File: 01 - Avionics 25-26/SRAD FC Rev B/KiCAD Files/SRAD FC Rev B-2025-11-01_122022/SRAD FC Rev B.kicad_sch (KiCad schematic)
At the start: 0 parts

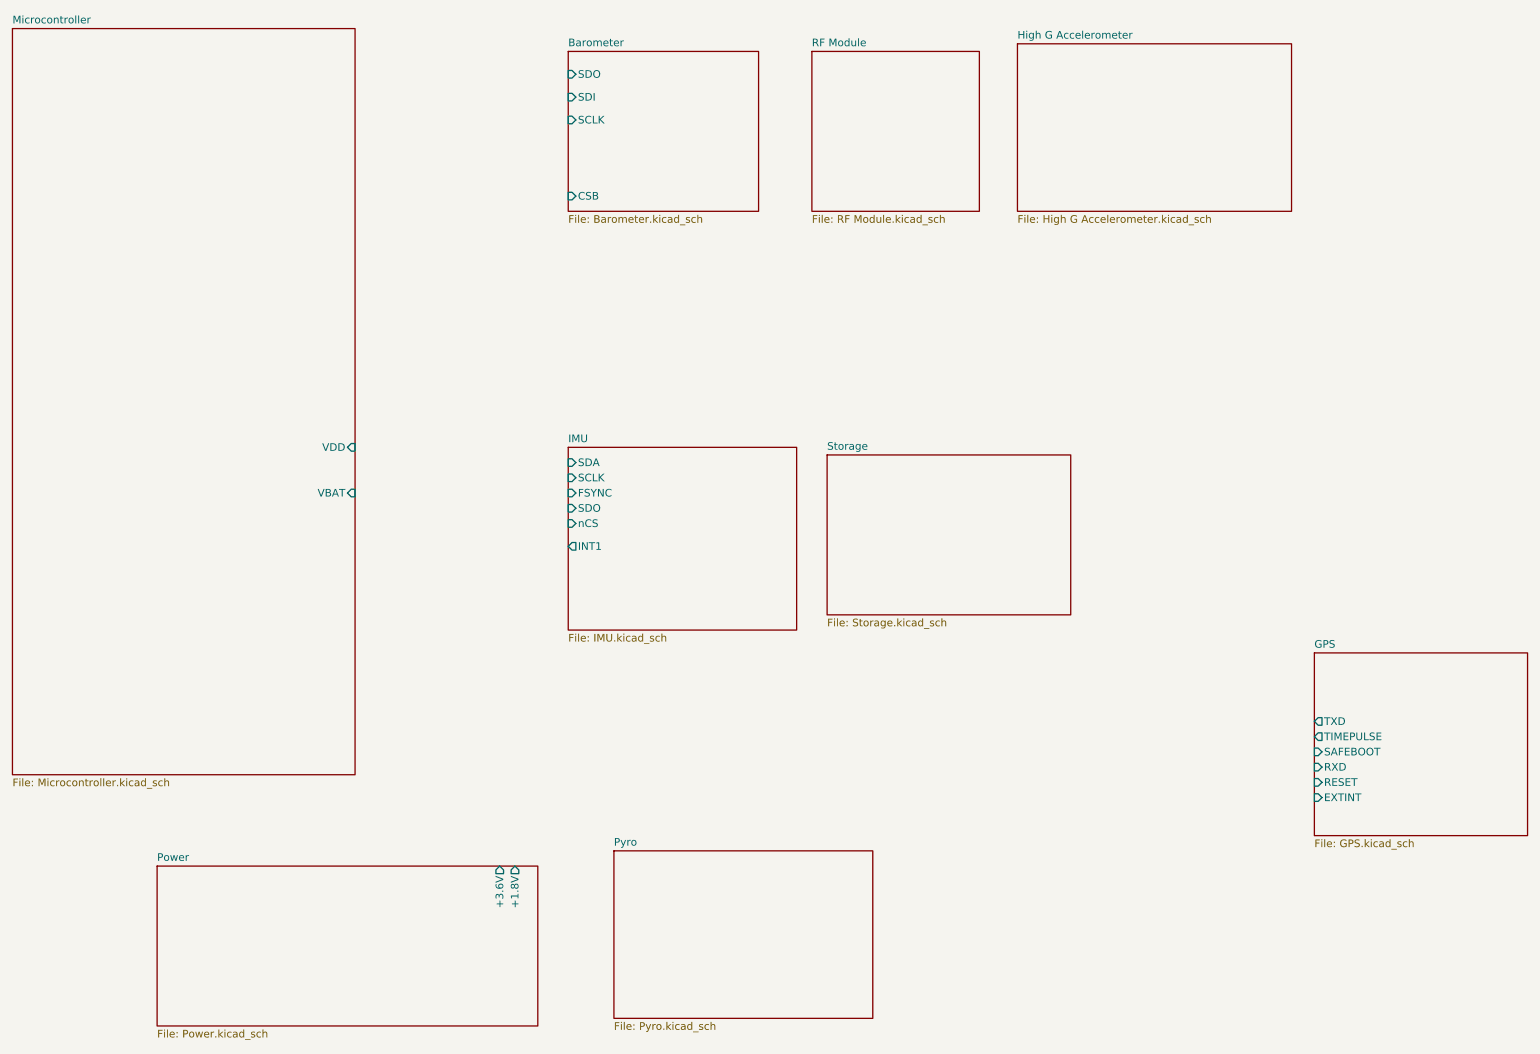
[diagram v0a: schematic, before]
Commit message: Added IMU and Barometer Circuits w/Root Symbols
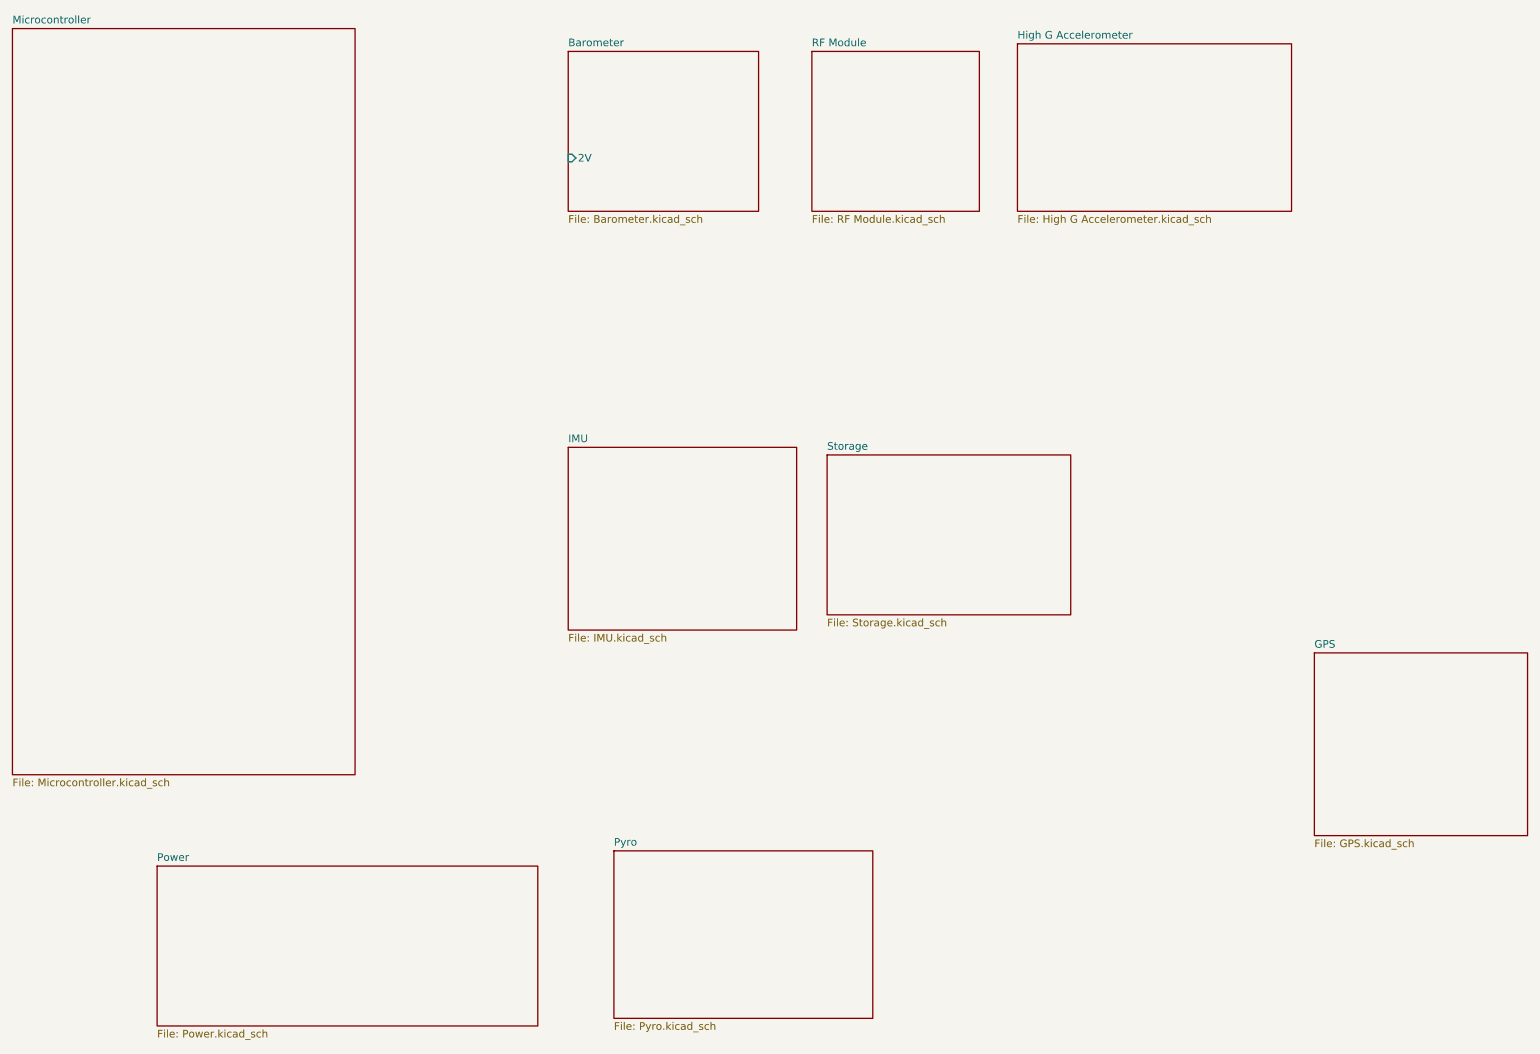
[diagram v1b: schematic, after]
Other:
- sheet Barometer ports: added 2V; removed CSB, SCLK, SDI, SDO
- sheet GPS ports: added none; removed EXTINT, RESET, RXD, SAFEBOOT, TIMEPULSE, TXD
- sheet IMU ports: added none; removed FSYNC, INT1, SCLK, SDA, SDO, nCS
- sheet Microcontroller ports: added none; removed VBAT, VDD
- sheet Power ports: added none; removed +1.8V, +3.6V
- company: Missouri S&T Rocket Design Team -> (none)
- title: SRAD FC Revision B -> (none)
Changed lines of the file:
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@@
 	(generator_version "9.0")
 	(paper "A4")
-	(title_block
-		(title "SRAD FC Revision B")
-		(date "2025-11-01")
-		(rev "B")
-		(company "Missouri S&T Rocket Design Team")
-		(comment 1 "Author(s): Aaron Brinker, Isaac Lough, Joseph Hinchie, Ryan Newey, and Ian Butrick")
-	)
 	(sheet
 		(at 45.72 162.56)
@@
 			)
 		)
-		(pin "+3.6V" output
-			(at 102.87 162.56 90)
-			(effects
-				(font
-					(size 1.27 1.27)
-				)
-				(justify right)
-			)
-		)
-		(pin "+1.8V" output
-			(at 105.41 162.56 90)
-			(effects
-				(font
-					(size 1.27 1.27)
-				)
-				(justify right)
-			)
-		)
 		(instances
 			(project "SRAD FC Rev B"
@@
 			)
 		)
-		(pin "VBAT" input
-			(at 78.74 100.33 0)
-			(effects
-				(font
-					(size 1.27 1.27)
-				)
-				(justify right)
-			)
-		)
-		(pin "VDD" input
-			(at 78.74 92.71 0)
-			(effects
-				(font
-					(size 1.27 1.27)
-				)
-				(justify right)
-			)
-		)
 		(instances
 			(project "SRAD FC Rev B"
@@
 			)
 		)
-		(pin "EXTINT" input
-			(at 238.76 151.13 180)
-			(effects
-				(font
-					(size 1.27 1.27)
-				)
-				(justify left)
-			)
-		)
-		(pin "RESET" input
-			(at 238.76 148.59 180)
-			(effects
-				(font
-					(size 1.27 1.27)
-				)
-				(justify left)
-			)
-		)
-		(pin "RXD" input
-			(at 238.76 146.05 180)
-			(effects
-				(font
-					(size 1.27 1.27)
-				)
-				(justify left)
-			)
-		)
-		(pin "SAFEBOOT" input
-			(at 238.76 143.51 180)
-			(effects
-				(font
-					(size 1.27 1.27)
-				)
-				(justify left)
-			)
-		)
-		(pin "TIMEPULSE" output
-			(at 238.76 140.97 180)
-			(effects
-				(font
-					(size 1.27 1.27)
-				)
-				(justify left)
-			)
-		)
-		(pin "TXD" output
-			(at 238.76 138.43 180)
-			(effects
-				(font
-					(size 1.27 1.27)
-				)
-				(justify left)
-			)
-		)
 		(instances
 			(project "SRAD FC Rev B"
@@
 			)
 		)
-		(pin "SDA" input
-			(at 114.3 95.25 180)
-			(effects
-				(font
-					(size 1.27 1.27)
-				)
-				(justify left)
-			)
-		)
-		(pin "SCLK" input
-			(at 114.3 97.79 180)
-			(effects
-				(font
-					(size 1.27 1.27)
-				)
-				(justify left)
-			)
-		)
-		(pin "FSYNC" input
-			(at 114.3 100.33 180)
-			(effects
-				(font
-					(size 1.27 1.27)
-				)
-				(justify left)
-			)
-		)
-		(pin "SDO" input
-			(at 114.3 102.87 180)
-			(effects
-				(font
-					(size 1.27 1.27)
-				)
-				(justify left)
-			)
-		)
-		(pin "INT1" output
-			(at 114.3 109.22 180)
-			(effects
-				(font
-					(size 1.27 1.27)
-				)
-				(justify left)
-			)
-		)
-		(pin "nCS" input
-			(at 114.3 105.41 180)
-			(effects
-				(font
-					(size 1.27 1.27)
-				)
-				(justify left)
-			)
-		)
 		(instances
 			(project "SRAD FC Rev B"
@@
 			)
 		)
-		(pin "SDO" input
-			(at 114.3 30.48 180)
-			(effects
-				(font
-					(size 1.27 1.27)
-				)
-				(justify left)
-			)
-		)
-		(pin "SDI" input
-			(at 114.3 34.29 180)
-			(effects
-				(font
-					(size 1.27 1.27)
-				)
-				(justify left)
-			)
-		)
-		(pin "CSB" input
-			(at 114.3 50.8 180)
-			(effects
-				(font
-					(size 1.27 1.27)
-				)
-				(justify left)
-			)
-		)
-		(pin "SCLK" input
-			(at 114.3 38.1 180)
-			(effects
-				(font
+		(pin "2V" input
+			(at 114.3 44.45 180)
+			(effects
+				(font
